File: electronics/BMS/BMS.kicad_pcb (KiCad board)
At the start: 2 copper layers, 8 parts

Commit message: adjusted the pcb
Original-author: Zachariah K. Sharma <zachariah.sharma@gmail.com>
Source-commit: d12762510ca6004b4800da7825b8d34d4b880e03
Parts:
- added R5: 5.1kΩ, PCM_JLCPCB:R_0402, F.Cu at (109.0, 76.2)
- added R6: 5.1kΩ, PCM_JLCPCB:R_0402, F.Cu at (109.0, 78.0)

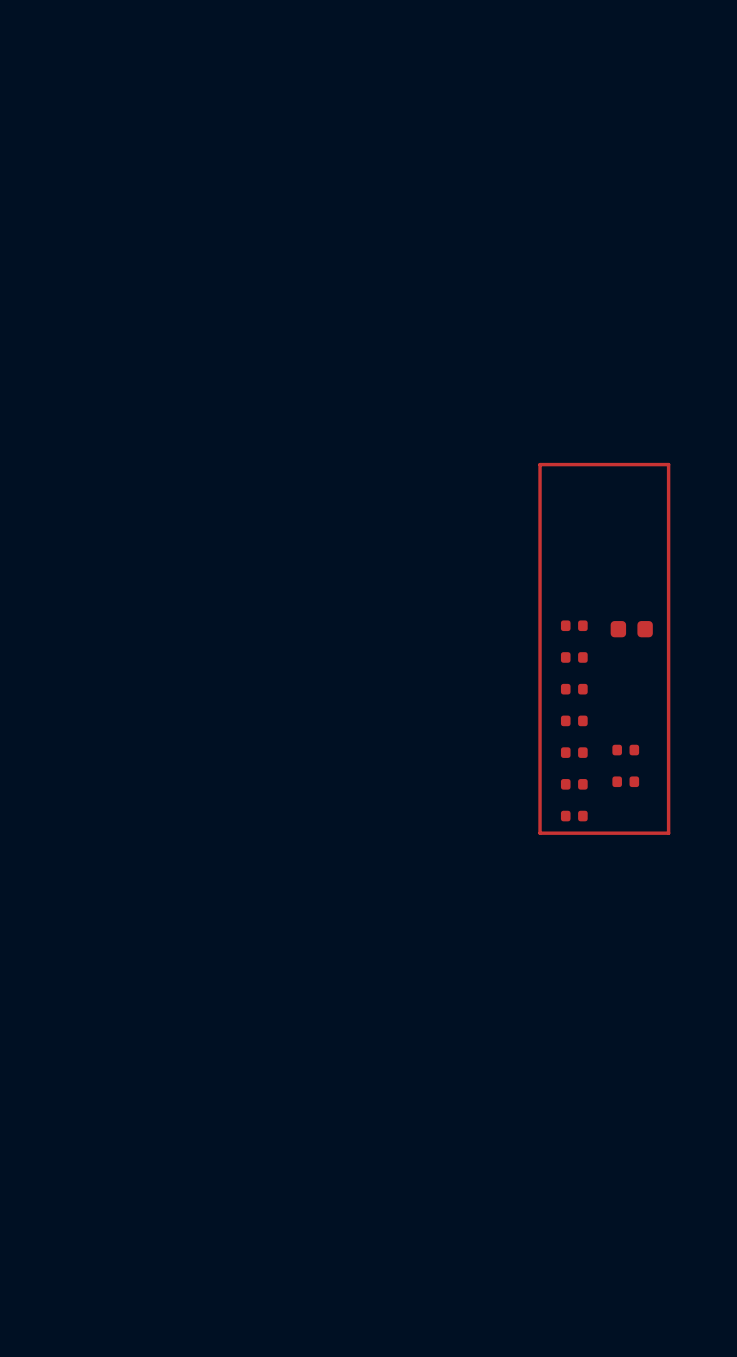
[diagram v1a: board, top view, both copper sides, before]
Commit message: Worked out the PCB Layout for the BMS, now I just need to size traces
Original-author: Zachariah K. Sharma <zachariah.sharma@gmail.com>
Source-commit: 28a479680107c7c66840ef810bf1f157462c39b5
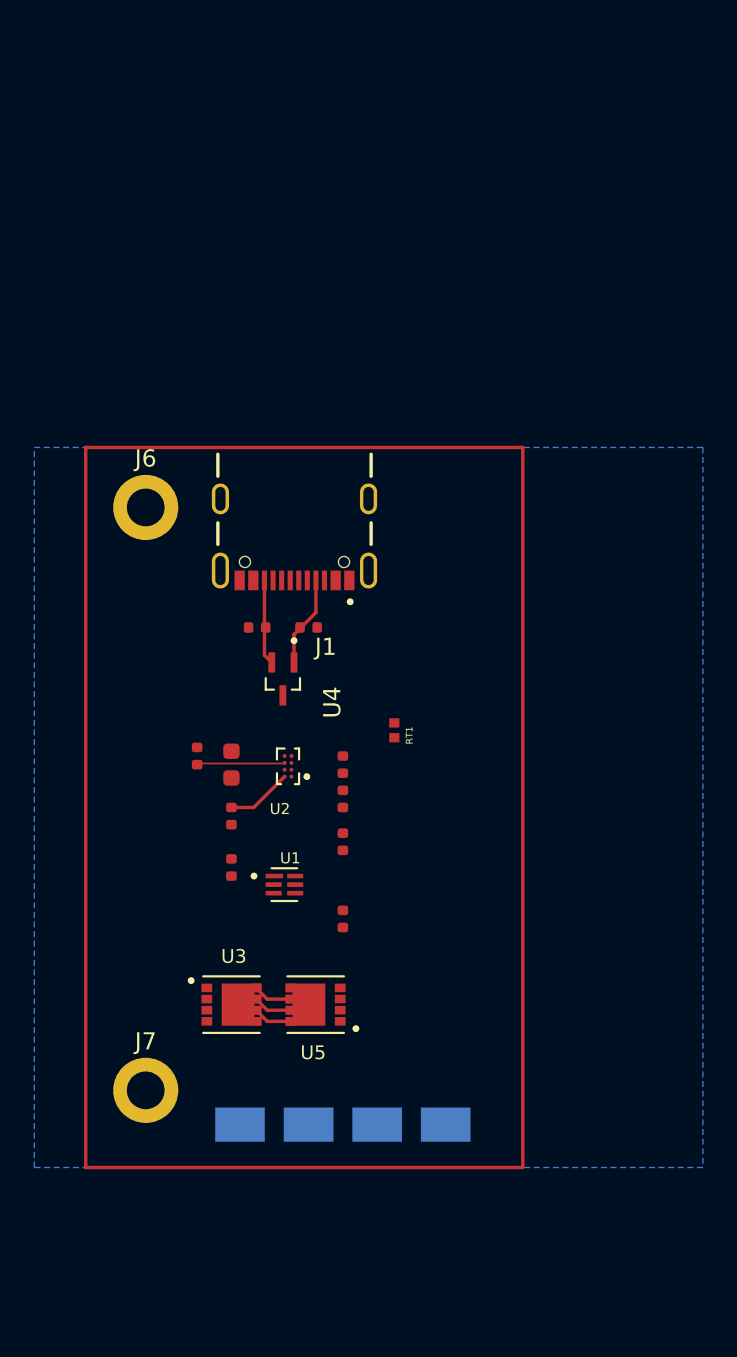
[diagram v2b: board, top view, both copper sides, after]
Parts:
- added J1: USB4105-GF-A, Footprints:GCT_USB4105-GF-A, F.Cu at (89.7, 61.5)
- added J2: S70-125161545R, Footprints:HARWIN_S70-125161545R, B.Cu at (98.5, 98.0)
- added J3: S70-125161545R, Footprints:HARWIN_S70-125161545R, B.Cu at (94.5, 98.0)
- added J4: S70-125161545R, Footprints:HARWIN_S70-125161545R, B.Cu at (90.5, 98.0)
- added J5: S70-125161545R, Footprints:HARWIN_S70-125161545R, B.Cu at (86.5, 98.0)
- added J6: Conn_01x01, MountingHole:MountingHole_2.2mm_M2_DIN965_Pad, F.Cu at (81.0, 62.0)
- added J7: Conn_01x01, MountingHole:MountingHole_2.2mm_M2_DIN965_Pad, F.Cu at (81.0, 96.0)
- added RT1: NCP15XH103F03RC, Footprints:THRMC1005X55N, F.Cu at (95.5, 75.0)
- added U1: BQ29700DSER, Footprints:SON50P150X150X80-6N, F.Cu at (89.1, 84.0)
- added U2: BQ25180YBGR, Footprints:IC_BQ25180YBGR, F.Cu at (89.3, 77.1)
- added U3: CSD16406Q3, Footprints:TRANS_CSD16406Q3, F.Cu at (86.0, 91.0)
- added U4: TPD2E2U06DCKR, Footprints:SOT65P210X110-3N, F.Cu at (89.0, 72.0)
- added U5: CSD16406Q3, Footprints:TRANS_CSD16406Q3, F.Cu at (90.9, 91.0)
- moved C2 24.7 mm to (86.0, 77.0), turned to 90 degrees
- moved R6 23.3 mm to (87.5, 69.0), turned to 180 degrees
- moved C4 22.3 mm to (84.0, 76.5), turned to -90 degrees
- moved C3 22.0 mm to (86.0, 80.0), turned to 90 degrees
- moved C1 21.8 mm to (92.5, 86.0), turned to -90 degrees
- moved R2 21.1 mm to (86.0, 83.0), turned to -90 degrees
- moved R5 19.8 mm to (90.5, 69.0), turned to 180 degrees
- moved R1 15.2 mm to (92.5, 81.5), turned to -90 degrees
- moved R4 13.8 mm to (92.5, 77.0), turned to 90 degrees
- moved R3 13.5 mm to (92.5, 79.0), turned to -90 degrees
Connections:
- C4 pad 2: PACK_P -> CELL+
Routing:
- net FET_MID: track 0.00 -> 6.93 mm
- net CC1: track 0.00 -> 5.31 mm
- net CELL+: track 0.00 -> 5.14 mm
- net CC2: track 0.00 -> 4.96 mm
- net VBUS: track 0.00 -> 3.82 mm
- added copper zone on B.Cu, net GND
- added copper zone on F.Cu, net SYS

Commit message: Traces seem decent, just working out some DRC problems
Original-author: Zachariah K. Sharma <zachariah.sharma@gmail.com>
Source-commit: 78d110570d095923f1a7908a118f83d782eac91c
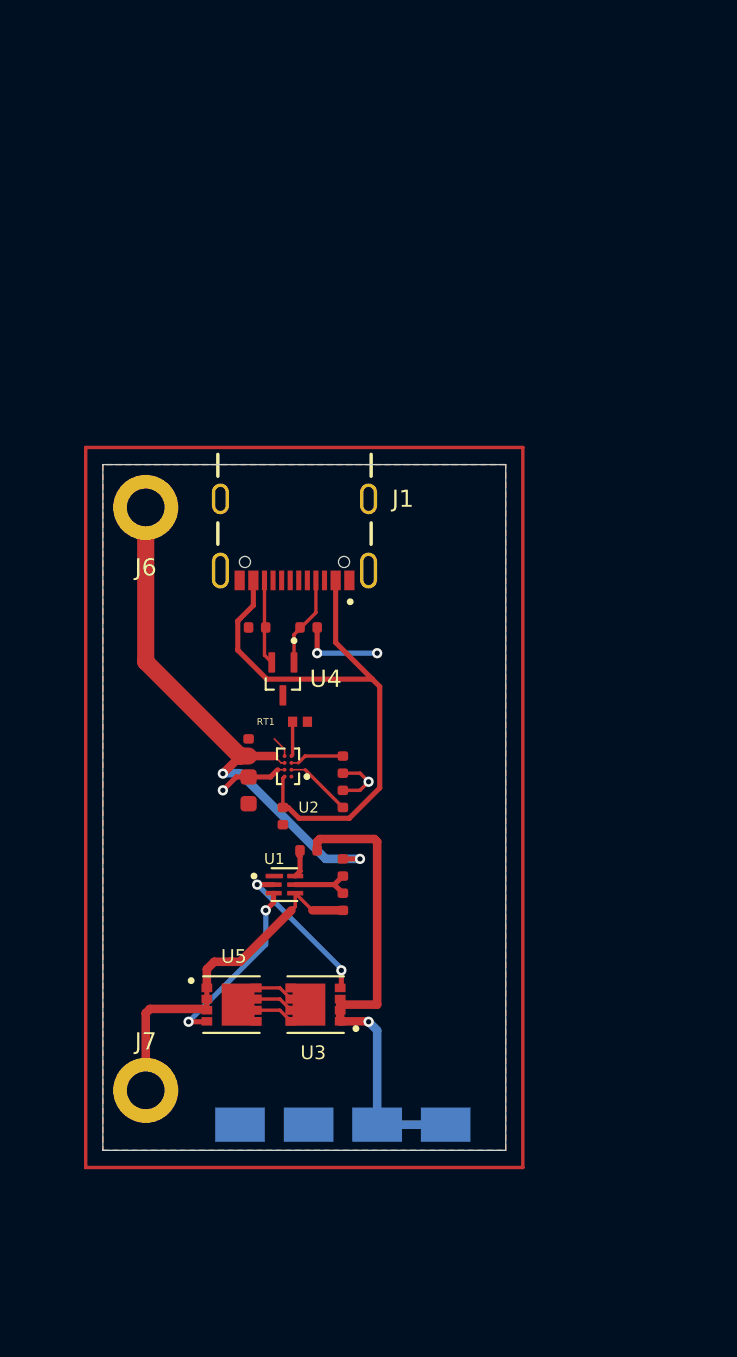
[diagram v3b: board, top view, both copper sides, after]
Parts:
- moved RT1 5.52 mm to (90.0, 74.5), turned to 0 degrees
- moved U3 4.91 mm to (90.9, 91.0), turned to 180 degrees
- moved U5 4.91 mm to (86.0, 91.0), turned to 0 degrees
- moved R2 4.61 mm to (90.5, 82.0), turned to 180 degrees
- moved C4 3.04 mm to (87.0, 76.0)
- moved C3 3.00 mm to (89.0, 80.0)
- moved C2 1.80 mm to (87.0, 78.5), turned to -90 degrees
- moved R1 1.50 mm to (92.5, 83.0)
- moved C1 1.00 mm to (92.5, 85.0), turned to 90 degrees
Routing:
- net VBUS: track 3.82 -> 34.6 mm
- net PACK-: track 0.00 -> 29.0 mm, vias 0 -> 1
- net CELL+: track 5.14 -> 32.1 mm, vias 0 -> 2
- net CELL-: track 0.00 -> 21.2 mm
- net DOUT: track 0.00 -> 10.6 mm, vias 0 -> 2
- net COUT: track 0.00 -> 9.05 mm, vias 0 -> 2
- net SYS: track 0.00 -> 7.51 mm, vias 0 -> 2
- net GND: track 0.00 -> 6.25 mm, vias 0 -> 2
- net Net-(U2-SCL): track 0.00 -> 3.91 mm
- net Net-(U1-BAT): track 0.00 -> 3.69 mm
- net Net-(U2-SDA): track 0.00 -> 3.17 mm
- net Net-(U2-TS/MR): track 0.00 -> 2.01 mm
- net Net-(U1-V-): track 0.00 -> 1.66 mm
- added copper zone on F.Cu, net GND
- added copper zone on B.Cu, net SYS
- removed copper zone on B.Cu, net GND
- removed copper zone on F.Cu, net SYS
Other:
- board outline added: 23.5 x 40 mm

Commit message: Finalized Everything for Review, exported gerbers
Original-author: Zachariah K. Sharma <zachariah.sharma@gmail.com>
Source-commit: 3e0c8e76005ef0c547eaa410b6d8aef809166c90
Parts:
- moved R5 24.5 mm to (90.8, 44.5)
- moved R6 24.5 mm to (87.8, 44.5)
- moved U4 24.5 mm to (89.3, 47.5)
- moved J6 24.5 mm to (81.3, 37.5)
- moved J1 24.4 mm to (90.0, 37.1)
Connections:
- J2 pad 1: PACK- -> GND
- J3 pad 1: PACK- -> GND
- R2 pad 1: PACK- -> GND
- U3 pad 1: PACK- -> GND
- U3 pad 2: PACK- -> GND
- U3 pad 3: PACK- -> GND
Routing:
- net PACK-: track 29.0 -> 0.00 mm, vias 1 -> 0
- net CELL+: track 32.1 -> 56.7 mm
- net VBUS: track 34.6 -> 55.2 mm
- net GND: track 6.25 -> 8.37 mm, vias 2 -> 1
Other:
- board size 23.5 x 40 mm -> 23.5 x 65 mm

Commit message: Autoprogramming, Finish off BMS, Add comps to Vent, and do a bunch of mobile stuff
Original-author: Zachariah K. Sharma <zachariah.sharma@gmail.com>
Source-commit: c8fb455aabb0719517b46fd9304eb5e5fb9f4004
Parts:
- J2, J3, J4, J5: footprint Footprints:HARWIN_S70-125161545R -> Footprints:ENIG_PAD
- moved J7 9.50 mm to (81.0, 105.5)
- moved J2 7.00 mm to (98.5, 105.0)
- moved J3 7.00 mm to (94.5, 105.0)
- moved J4 7.00 mm to (90.5, 105.0)
- moved J5 7.00 mm to (86.5, 105.0)
- moved J1 2.90 mm to (90.0, 40.0)
- moved J6 2.90 mm to (81.3, 40.4)
- moved R5 2.90 mm to (90.8, 47.4)
- moved R6 2.90 mm to (87.8, 47.4)
- moved U4 2.90 mm to (89.3, 50.4)
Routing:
- net CELL-: track 21.2 -> 30.7 mm
- net VBUS: track 55.2 -> 52.3 mm
- net CELL+: track 56.7 -> 53.8 mm
- net GND: track 8.37 -> 6.87 mm
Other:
- board size 23.5 x 65 mm -> 23.5 x 72.1 mm
- board text added: "C1"
- board text added: "C2"
- board text added: "C3"
- board text added: "C4"
- board text added: "R1"
- board text added: "R2"
- board text added: "R3"
- board text added: "R4"
- board text added: "R5"
- board text added: "R6"
- board text added: "U5"
